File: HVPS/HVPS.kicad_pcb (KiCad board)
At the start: 2 copper layers, 18 x 18 mm, 9 parts, among them Q1 2SD2470, T1 Flash XFMR

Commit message: Add files via upload
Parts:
- renumbered GND1 to GND
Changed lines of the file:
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@@
     (0 F.Cu signal)
     (31 B.Cu signal)
-    (32 B.Adhes user)
-    (33 F.Adhes user)
+    (32 B.Adhes user hide)
+    (33 F.Adhes user hide)
     (34 B.Paste user)
     (35 F.Paste user)
@@
     (38 B.Mask user)
     (39 F.Mask user)
-    (40 Dwgs.User user)
-    (41 Cmts.User user)
-    (42 Eco1.User user)
-    (43 Eco2.User user)
+    (40 Dwgs.User user hide)
+    (41 Cmts.User user hide)
+    (42 Eco1.User user hide)
+    (43 Eco2.User user hide)
     (44 Edge.Cuts user)
-    (45 Margin user)
-    (46 B.CrtYd user)
-    (47 F.CrtYd user)
+    (45 Margin user hide)
+    (46 B.CrtYd user hide)
+    (47 F.CrtYd user hide)
     (48 B.Fab user hide)
     (49 F.Fab user hide)
@@
       (outputformat 1)
       (mirror false)
-      (drillshape 1)
+      (drillshape 0)
       (scaleselection 1)
-      (outputdirectory ""))
+      (outputdirectory "./"))
   )
   (net 0 "")
@@
     (tags connector)
     (attr virtual)
-    (fp_text reference GND1 (at 1.97104 0.02794 270) (layer F.SilkS)
+    (fp_text reference GND (at 1.97104 0.02794 270) (layer F.SilkS)
       (effects (font (size 0.5 0.5) (thickness 0.125)))
     )
@@
     (effects (font (size 0.5 0.5) (thickness 0.125)))
   )
-  (gr_text "this side down" (at 139.82192 109.74324 90) (layer F.SilkS)
+  (gr_text "this side down" (at 138.5316 109.601 90) (layer F.SilkS)
     (effects (font (size 0.5 0.5) (thickness 0.125)))
   )

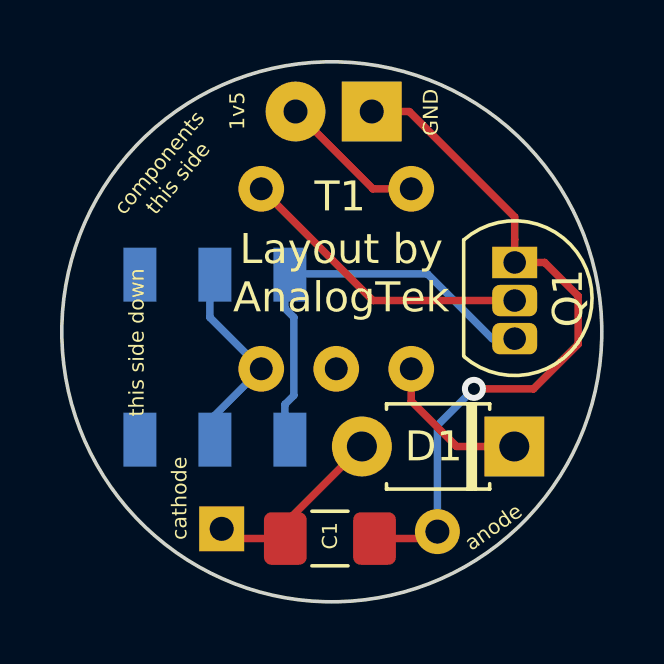
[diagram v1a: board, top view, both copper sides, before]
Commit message: Add files via upload
15 NOV 2020 11:06 PM changed trace width from .25mm to .4 - .75mm.
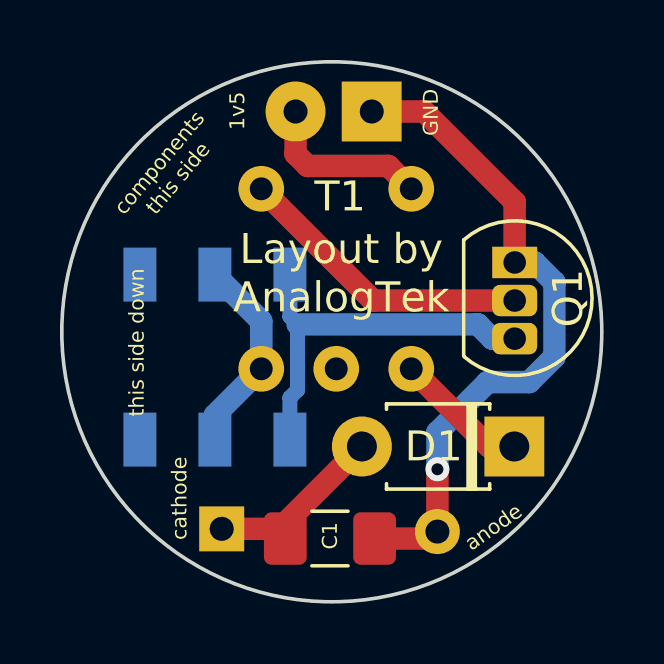
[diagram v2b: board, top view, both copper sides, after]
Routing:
- net Net-(Q1-Pad3): track 14.3 -> 13.1 mm
- net GND: track 23.5 -> 22.6 mm
- net +1V5: track 4.92 -> 5.75 mm
- net Net-(D1-Pad1): track 5.14 -> 4.51 mm
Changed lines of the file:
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@@
   )
   (setup
-    (last_trace_width 0.25)
+    (last_trace_width 0.75)
     (user_trace_width 0.5)
     (user_trace_width 0.75)
@@
     (effects (font (size 1 1) (thickness 0.125)))
   )
-  (segment (start 151.13 106.159) (end 151.13 106.934) (width 0.25) (layer F.Cu) (net 1))
-  (segment (start 147.61445 101.90226) (end 151.13 105.41781) (width 0.25) (layer F.Cu) (net 1))
-  (segment (start 151.13 105.41781) (end 151.13 106.159) (width 0.25) (layer F.Cu) (net 1))
-  (segment (start 146.36496 101.90226) (end 147.61445 101.90226) (width 0.25) (layer F.Cu) (net 1))
-  (segment (start 148.3233 116.13642) (end 148.55444 115.90528) (width 0.25) (layer F.Cu) (net 1))
-  (segment (start 146.4596 116.13642) (end 148.3233 116.13642) (width 0.25) (layer F.Cu) (net 1))
-  (segment (start 152.13 106.934) (end 153.24582 108.04982) (width 0.25) (layer F.Cu) (net 1))
-  (segment (start 151.13 106.934) (end 152.13 106.934) (width 0.25) (layer F.Cu) (net 1))
-  (segment (start 153.24582 108.04982) (end 153.24582 109.65942) (width 0.25) (layer F.Cu) (net 1))
-  (segment (start 153.24582 109.65942) (end 151.75738 111.14786) (width 0.25) (layer F.Cu) (net 1))
-  (via (at 149.7711 111.14786) (size 0.8) (drill 0.4) (layers F.Cu B.Cu) (net 1))
-  (segment (start 151.75738 111.14786) (end 149.7711 111.14786) (width 0.25) (layer F.Cu) (net 1))
-  (segment (start 148.55444 112.36452) (end 148.55444 115.90528) (width 0.25) (layer B.Cu) (net 1))
-  (segment (start 149.7711 111.14786) (end 148.55444 112.36452) (width 0.25) (layer B.Cu) (net 1))
-  (segment (start 150.38 109.474) (end 151.13 109.474) (width 0.25) (layer B.Cu) (net 2))
-  (segment (start 148.221 107.315) (end 150.38 109.474) (width 0.25) (layer B.Cu) (net 2))
-  (segment (start 143.4719 107.315) (end 148.221 107.315) (width 0.25) (layer B.Cu) (net 2))
-  (segment (start 143.4719 111.665) (end 143.4719 112.815) (width 0.25) (layer B.Cu) (net 2))
-  (segment (start 143.768961 111.367939) (end 143.4719 111.665) (width 0.25) (layer B.Cu) (net 2))
-  (segment (start 143.768961 108.762061) (end 143.768961 111.367939) (width 0.25) (layer B.Cu) (net 2))
-  (segment (start 143.4719 108.465) (end 143.768961 108.762061) (width 0.25) (layer B.Cu) (net 2))
-  (segment (start 143.4719 107.315) (end 143.4719 108.465) (width 0.25) (layer B.Cu) (net 2))
-  (segment (start 146.40688 108.204) (end 151.13 108.204) (width 0.25) (layer F.Cu) (net 3))
-  (segment (start 142.68196 104.47908) (end 146.40688 108.204) (width 0.25) (layer F.Cu) (net 3))
-  (segment (start 146.40178 104.47908) (end 147.68196 104.47908) (width 0.25) (layer F.Cu) (net 4))
-  (segment (start 143.82496 101.90226) (end 146.40178 104.47908) (width 0.25) (layer F.Cu) (net 4))
-  (segment (start 143.4846 115.6208) (end 143.4846 116.13642) (width 0.25) (layer F.Cu) (net 5))
-  (segment (start 146.0373 113.0681) (end 143.4846 115.6208) (width 0.25) (layer F.Cu) (net 5))
-  (segment (start 141.68628 116.13642) (end 141.3637 115.81384) (width 0.25) (layer F.Cu) (net 5))
-  (segment (start 143.4846 116.13642) (end 141.68628 116.13642) (width 0.25) (layer F.Cu) (net 5))
-  (segment (start 149.19335 113.0681) (end 149.8673 113.0681) (width 0.25) (layer F.Cu) (net 6))
-  (segment (start 149.8673 113.0681) (end 151.1173 113.0681) (width 0.25) (layer F.Cu) (net 6))
-  (segment (start 147.68196 111.55671) (end 149.19335 113.0681) (width 0.25) (layer F.Cu) (net 6))
-  (segment (start 147.68196 110.47908) (end 147.68196 111.55671) (width 0.25) (layer F.Cu) (net 6))
-  (segment (start 140.9719 108.76902) (end 142.68196 110.47908) (width 0.25) (layer B.Cu) (net 7))
-  (segment (start 140.9719 107.315) (end 140.9719 108.76902) (width 0.25) (layer B.Cu) (net 7))
-  (segment (start 140.9719 112.18914) (end 140.9719 112.815) (width 0.25) (layer B.Cu) (net 7))
-  (segment (start 142.68196 110.47908) (end 140.9719 112.18914) (width 0.25) (layer B.Cu) (net 7))
+  (segment (start 148.11445 101.90226) (end 146.36496 101.90226) (width 0.75) (layer F.Cu) (net 1))
+  (segment (start 151.13 104.91781) (end 148.11445 101.90226) (width 0.75) (layer F.Cu) (net 1))
+  (segment (start 151.13 106.934) (end 151.13 104.91781) (width 0.75) (layer F.Cu) (net 1))
+  (segment (start 148.3233 116.13642) (end 148.55444 115.90528) (width 0.75) (layer F.Cu) (net 1))
+  (segment (start 146.4596 116.13642) (end 148.3233 116.13642) (width 0.75) (layer F.Cu) (net 1))
+  (segment (start 148.55444 115.90528) (end 148.55444 113.82756) (width 0.75) (layer F.Cu) (net 1))
+  (via (at 148.55444 113.82756) (size 0.8) (drill 0.4) (layers F.Cu B.Cu) (net 1))
+  (segment (start 148.55444 112.595958) (end 150.228598 110.9218) (width 0.75) (layer B.Cu) (net 1))
+  (segment (start 148.55444 113.82756) (end 148.55444 112.595958) (width 0.75) (layer B.Cu) (net 1))
+  (segment (start 151.79442 106.934) (end 151.13 106.934) (width 0.75) (layer B.Cu) (net 1))
+  (segment (start 152.45501 107.59459) (end 151.79442 106.934) (width 0.75) (layer B.Cu) (net 1))
+  (segment (start 151.61662 110.9218) (end 152.45501 110.08341) (width 0.75) (layer B.Cu) (net 1))
+  (segment (start 152.45501 110.08341) (end 152.45501 107.59459) (width 0.75) (layer B.Cu) (net 1))
+  (segment (start 150.228598 110.9218) (end 151.61662 110.9218) (width 0.75) (layer B.Cu) (net 1))
+  (segment (start 143.893961 111.183439) (end 143.893961 108.997361) (width 0.5) (layer B.Cu) (net 2))
+  (segment (start 143.637 111.4404) (end 143.893961 111.183439) (width 0.5) (layer B.Cu) (net 2))
+  (segment (start 143.637 108.7404) (end 143.637 107.3404) (width 0.5) (layer B.Cu) (net 2))
+  (segment (start 143.893961 108.997361) (end 143.637 108.7404) (width 0.5) (layer B.Cu) (net 2))
+  (segment (start 143.637 112.8404) (end 143.637 111.4404) (width 0.5) (layer B.Cu) (net 2))
+  (segment (start 150.38 109.474) (end 151.13 109.474) (width 0.75) (layer B.Cu) (net 2))
+  (segment (start 149.903361 108.997361) (end 150.38 109.474) (width 0.75) (layer B.Cu) (net 2))
+  (segment (start 143.893961 108.997361) (end 149.903361 108.997361) (width 0.75) (layer B.Cu) (net 2))
+  (segment (start 146.40688 108.204) (end 151.13 108.204) (width 0.75) (layer F.Cu) (net 3))
+  (segment (start 142.68196 104.47908) (end 146.40688 108.204) (width 0.75) (layer F.Cu) (net 3))
+  (segment (start 143.82496 103.315752) (end 143.82496 101.90226) (width 0.75) (layer F.Cu) (net 4))
+  (segment (start 144.226289 103.717081) (end 143.82496 103.315752) (width 0.75) (layer F.Cu) (net 4))
+  (segment (start 147.68196 104.47908) (end 146.919961 103.717081) (width 0.75) (layer F.Cu) (net 4))
+  (segment (start 146.919961 103.717081) (end 144.226289 103.717081) (width 0.75) (layer F.Cu) (net 4))
+  (segment (start 143.16202 115.81384) (end 143.4846 116.13642) (width 0.75) (layer F.Cu) (net 5))
+  (segment (start 141.3637 115.81384) (end 143.16202 115.81384) (width 0.75) (layer F.Cu) (net 5))
+  (segment (start 143.4846 115.6208) (end 146.0373 113.0681) (width 0.75) (layer F.Cu) (net 5))
+  (segment (start 143.4846 116.13642) (end 143.4846 115.6208) (width 0.75) (layer F.Cu) (net 5))
+  (segment (start 150.27098 113.0681) (end 147.68196 110.47908) (width 0.75) (layer F.Cu) (net 6))
+  (segment (start 151.1173 113.0681) (end 150.27098 113.0681) (width 0.75) (layer F.Cu) (net 6))
+  (segment (start 141.137 112.02404) (end 142.68196 110.47908) (width 0.75) (layer B.Cu) (net 7))
+  (segment (start 141.137 112.8404) (end 141.137 112.02404) (width 0.75) (layer B.Cu) (net 7))
+  (segment (start 142.68196 108.88536) (end 141.137 107.3404) (width 0.75) (layer B.Cu) (net 7))
+  (segment (start 142.68196 110.47908) (end 142.68196 108.88536) (width 0.75) (layer B.Cu) (net 7))
 )
